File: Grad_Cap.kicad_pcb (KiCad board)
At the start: 2 copper layers, 339.4 x 339.4 mm, 89 parts, among them U1 ItsyBitsy 32u4 5V

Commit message: routing time
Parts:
- moved U1 48.4 mm to (202.5, 220.0), turned to 0 degrees
- renumbered D71 to D1, D4 to D10, D5 to D11, D7 to D12, D8 to D13, D9 to D14, D64 to D15, D63 to D16, D62 to D17, D61 to D18, D60 to D19, D70 to D2, D59 to D20, D58 to D21, D57 to D22, D56 to D23, D55 to D24, D54 to D25, D52 to D26, D51 to D27, D49 to D28, D48 to D29, D69 to D3, D48 to D30, D46 to D31, D45 to D32, D44 to D33, D43 to D34, D41 to D35, D40 to D36, D39 to D37, D37 to D39, D68 to D4, D36 to D40, D35 to D41, D33 to D42, D32 to D43, D31 to D44, D30 to D45, D29 to D46, D28 to D47, D27 to D48, D25 to D49, D67 to D5, D24 to D50, D23 to D51, D22 to D52, D21 to D53, D20 to D54, D19 to D55, D17 to D56, D16 to D57, D15 to D58, D14 to D59, D66 to D6, D13 to D60, D7 to D61, D8 to D62, D10 to D63, D11 to D64, D12 to D65, D1 to D66, D1 to D67, D65 to D68, D9 to D69, D65 to D7, D66 to D70, D65 to D71, D9 to D72, D66 to D73, D67 to D74, D9 to D75, D8 to D76, D7 to D77, D9 to D78, D9 to D79, D1 to D8, D9 to D80, D9 to D81, D9 to D82, D8 to D83, D7 to D84, D8 to D85, D3 to D9
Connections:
- D1 pad 2: Net-(D70-Pad4) -> Net-(D1-Pad2)
- D1 pad 4: Net-(D71-Pad4) -> Net-(D1-Pad4)
- D11 pad 4: Net-(D5-Pad4) -> Net-(D11-Pad4)
- D12 pad 2: Net-(D6-Pad4) -> Net-(D11-Pad4)
- D12 pad 4: Net-(D7-Pad4) -> Net-(D12-Pad4)
- D13 pad 2: Net-(D7-Pad4) -> Net-(D12-Pad4)
- D13 pad 4: Net-(D8-Pad4) -> Net-(D13-Pad4)
- D14 pad 1: (no net) -> GND
- D14 pad 2: (no net) -> Net-(D13-Pad4)
- D14 pad 3: (no net) -> +5V
- D14 pad 4: (no net) -> Net-(D14-Pad4)
- D15 pad 2: Net-(D63-Pad4) -> Net-(D14-Pad4)
- D15 pad 4: Net-(D64-Pad4) -> Net-(D15-Pad4)
- D16 pad 2: Net-(D62-Pad4) -> Net-(D15-Pad4)
- D16 pad 4: Net-(D63-Pad4) -> Net-(D16-Pad4)
- D17 pad 2: Net-(D61-Pad4) -> Net-(D16-Pad4)
- D17 pad 4: Net-(D62-Pad4) -> Net-(D17-Pad4)
- D18 pad 2: Net-(D60-Pad4) -> Net-(D17-Pad4)
- D18 pad 4: Net-(D61-Pad4) -> Net-(D18-Pad4)
- D19 pad 2: Net-(D59-Pad4) -> Net-(D18-Pad4)
- D19 pad 4: Net-(D60-Pad4) -> Net-(D19-Pad4)
- D2 pad 2: Net-(D69-Pad4) -> Net-(D1-Pad4)
- D2 pad 4: Net-(D70-Pad4) -> Net-(D2-Pad4)
- D20 pad 2: Net-(D58-Pad4) -> Net-(D19-Pad4)
- D20 pad 4: Net-(D59-Pad4) -> Net-(D20-Pad4)
- D21 pad 2: Net-(D57-Pad4) -> Net-(D20-Pad4)
- D21 pad 4: Net-(D58-Pad4) -> Net-(D21-Pad4)
- D22 pad 2: Net-(D56-Pad4) -> Net-(D21-Pad4)
- D22 pad 4: Net-(D57-Pad4) -> Net-(D22-Pad4)
- D23 pad 2: Net-(D55-Pad4) -> Net-(D22-Pad4)
- D23 pad 4: Net-(D56-Pad4) -> Net-(D23-Pad4)
- D24 pad 2: Net-(D54-Pad4) -> Net-(D23-Pad4)
- D24 pad 4: Net-(D55-Pad4) -> Net-(D24-Pad4)
- D25 pad 2: Net-(D53-Pad4) -> Net-(D24-Pad4)
- D25 pad 4: Net-(D54-Pad4) -> Net-(D25-Pad4)
- D26 pad 2: Net-(D51-Pad4) -> Net-(D25-Pad4)
- D26 pad 4: Net-(D52-Pad4) -> Net-(D26-Pad4)
- D27 pad 2: Net-(D50-Pad4) -> Net-(D26-Pad4)
- D27 pad 4: Net-(D51-Pad4) -> Net-(D27-Pad4)
- D28 pad 2: Net-(D48-Pad4) -> Net-(D27-Pad4)
- D28 pad 4: Net-(D49-Pad4) -> Net-(D28-Pad4)
- D29 pad 2: Net-(D47-Pad4) -> Net-(D28-Pad4)
- D29 pad 4: Net-(D48-Pad4) -> Net-(D29-Pad4)
- D3 pad 2: Net-(D68-Pad4) -> Net-(D2-Pad4)
- D3 pad 4: Net-(D69-Pad4) -> Net-(D3-Pad4)
- D30 pad 1: (no net) -> GND
- D30 pad 2: (no net) -> Net-(D29-Pad4)
- D30 pad 3: (no net) -> +5V
- D30 pad 4: (no net) -> Net-(D30-Pad4)
- D31 pad 2: Net-(D45-Pad4) -> Net-(D30-Pad4)
- D31 pad 4: Net-(D46-Pad4) -> Net-(D31-Pad4)
- D32 pad 2: Net-(D44-Pad4) -> Net-(D31-Pad4)
- D32 pad 4: Net-(D45-Pad4) -> Net-(D32-Pad4)
- D33 pad 2: Net-(D43-Pad4) -> Net-(D32-Pad4)
- D33 pad 4: Net-(D44-Pad4) -> Net-(D33-Pad4)
- D34 pad 2: Net-(D42-Pad4) -> Net-(D33-Pad4)
- D34 pad 4: Net-(D43-Pad4) -> Net-(D34-Pad4)
- D35 pad 2: Net-(D40-Pad4) -> Net-(D34-Pad4)
- D35 pad 4: Net-(D41-Pad4) -> Net-(D35-Pad4)
- D36 pad 2: Net-(D39-Pad4) -> Net-(D35-Pad4)
- D36 pad 4: Net-(D40-Pad4) -> Net-(D36-Pad4)
- D37 pad 2: Net-(D38-Pad4) -> Net-(D36-Pad4)
- D37 pad 4: Net-(D39-Pad4) -> Net-(D37-Pad4)
- D39 pad 2: Net-(D36-Pad4) -> Net-(D38-Pad4)
- D39 pad 4: Net-(D37-Pad4) -> Net-(D39-Pad4)
- D4 pad 2: Net-(D67-Pad4) -> Net-(D3-Pad4)
- D4 pad 4: Net-(D68-Pad4) -> Net-(D4-Pad4)
- D40 pad 2: Net-(D35-Pad4) -> Net-(D39-Pad4)
- D40 pad 4: Net-(D36-Pad4) -> Net-(D40-Pad4)
- D41 pad 2: Net-(D34-Pad4) -> Net-(D40-Pad4)
- D41 pad 4: Net-(D35-Pad4) -> Net-(D41-Pad4)
- D42 pad 2: Net-(D32-Pad4) -> Net-(D41-Pad4)
- D42 pad 4: Net-(D33-Pad4) -> Net-(D42-Pad4)
- D43 pad 2: Net-(D31-Pad4) -> Net-(D42-Pad4)
- D43 pad 4: Net-(D32-Pad4) -> Net-(D43-Pad4)
- D44 pad 2: Net-(D30-Pad4) -> Net-(D43-Pad4)
- D44 pad 4: Net-(D31-Pad4) -> Net-(D44-Pad4)
- D45 pad 2: Net-(D29-Pad4) -> Net-(D44-Pad4)
- D45 pad 4: Net-(D30-Pad4) -> Net-(D45-Pad4)
- D46 pad 2: Net-(D28-Pad4) -> Net-(D45-Pad4)
- D46 pad 4: Net-(D29-Pad4) -> Net-(D46-Pad4)
- D47 pad 2: Net-(D27-Pad4) -> Net-(D46-Pad4)
- D47 pad 4: Net-(D28-Pad4) -> Net-(D47-Pad4)
- D48 pad 2: Net-(D26-Pad4) -> Net-(D47-Pad4)
- D48 pad 4: Net-(D27-Pad4) -> Net-(D48-Pad4)
- D49 pad 2: Net-(D24-Pad4) -> Net-(D48-Pad4)
- D49 pad 4: Net-(D25-Pad4) -> Net-(D49-Pad4)
- D5 pad 2: Net-(D66-Pad4) -> Net-(D4-Pad4)
- D5 pad 4: Net-(D67-Pad4) -> Net-(D5-Pad4)
- D50 pad 2: Net-(D23-Pad4) -> Net-(D49-Pad4)
- D50 pad 4: Net-(D24-Pad4) -> Net-(D50-Pad4)
- D51 pad 1: (no net) -> GND
- D51 pad 2: (no net) -> Net-(D50-Pad4)
- D51 pad 3: (no net) -> +5V
- D51 pad 4: (no net) -> Net-(D51-Pad4)
- D52 pad 2: Net-(D21-Pad4) -> Net-(D51-Pad4)
- D52 pad 4: Net-(D22-Pad4) -> Net-(D52-Pad4)
- D53 pad 2: Net-(D20-Pad4) -> Net-(D52-Pad4)
- D53 pad 4: Net-(D21-Pad4) -> Net-(D53-Pad4)
- D54 pad 2: Net-(D19-Pad4) -> Net-(D53-Pad4)
- D54 pad 4: Net-(D20-Pad4) -> Net-(D54-Pad4)
- D55 pad 2: Net-(D18-Pad4) -> Net-(D54-Pad4)
- D55 pad 4: Net-(D19-Pad4) -> Net-(D55-Pad4)
- D56 pad 2: Net-(D16-Pad4) -> Net-(D55-Pad4)
- D56 pad 4: Net-(D17-Pad4) -> Net-(D56-Pad4)
- D57 pad 2: Net-(D15-Pad4) -> Net-(D56-Pad4)
- D57 pad 4: Net-(D16-Pad4) -> Net-(D57-Pad4)
- D58 pad 2: Net-(D14-Pad4) -> Net-(D57-Pad4)
- D58 pad 4: Net-(D15-Pad4) -> Net-(D58-Pad4)
- D59 pad 2: Net-(D13-Pad4) -> Net-(D58-Pad4)
- D59 pad 4: Net-(D14-Pad4) -> Net-(D59-Pad4)
- D6 pad 2: Net-(D65-Pad4) -> Net-(D5-Pad4)
- D6 pad 4: Net-(D66-Pad4) -> Net-(D6-Pad4)
- D60 pad 2: Net-(D12-Pad4) -> Net-(D59-Pad4)
- D60 pad 4: Net-(D13-Pad4) -> Net-(D60-Pad4)
- D61 pad 2: Net-(D6-Pad4) -> Net-(D60-Pad4)
- D61 pad 4: Net-(D7-Pad4) -> Net-(D61-Pad4)
- D62 pad 2: Net-(D7-Pad4) -> Net-(D61-Pad4)
- D62 pad 4: Net-(D8-Pad4) -> Net-(D62-Pad4)
- D63 pad 2: Net-(D10-Pad2) (its old number) -> Net-(D62-Pad4)
- D63 pad 4: Net-(D10-Pad4) (its old number) -> Net-(D63-Pad4)
- D64 pad 1: (no net) -> GND
- D64 pad 2: (no net) -> Net-(D63-Pad4)
- D64 pad 3: (no net) -> +5V
- D64 pad 4: (no net) -> Net-(D64-Pad4)
- D65 pad 2: Net-(D11-Pad4) -> Net-(D64-Pad4)
- D65 pad 4: Net-(D12-Pad4) -> Net-(D65-Pad4)
- D66 pad 1: (no net) -> GND
- D66 pad 2: (no net) -> Net-(D65-Pad4)
- D66 pad 3: (no net) -> +5V
- D66 pad 4: (no net) -> Net-(D66-Pad4)
- D67 pad 1: (no net) -> GND
- D67 pad 2: (no net) -> Net-(D66-Pad4)
- D67 pad 3: (no net) -> +5V
- D67 pad 4: (no net) -> Net-(D67-Pad4)
- D68 pad 2: Net-(D64-Pad4) -> Net-(D67-Pad4)
- D68 pad 4: Net-(D65-Pad4) -> Net-(D68-Pad4)
- D69 pad 1: (no net) -> GND
- D69 pad 2: (no net) -> Net-(D68-Pad4)
- D69 pad 3: (no net) -> +5V
- D69 pad 4: (no net) -> Net-(D69-Pad4)
- D7 pad 2: Net-(D64-Pad4) -> Net-(D6-Pad4)
- D7 pad 4: Net-(D65-Pad4) -> Net-(D7-Pad4)
- D70 pad 2: Net-(D65-Pad4) -> Net-(D69-Pad4)
- D70 pad 4: Net-(D66-Pad4) -> Net-(D70-Pad4)
- D71 pad 2: Net-(D64-Pad4) -> Net-(D70-Pad4)
- D71 pad 4: Net-(D65-Pad4) -> Net-(D71-Pad4)
- D72 pad 1: (no net) -> GND
- D72 pad 2: (no net) -> Net-(D71-Pad4)
- D72 pad 3: (no net) -> +5V
- D72 pad 4: (no net) -> unconnected-(D72-Pad4)
- D8 pad 2: Net-(D1-Pad2) -> Net-(D7-Pad4)
- D8 pad 4: Net-(D1-Pad4) -> Net-(D8-Pad4)
- D9 pad 2: Net-(D2-Pad4) -> Net-(D8-Pad4)
- R1 pad 1: Net-(R1-Pad1) -> Net-(U1-Pad19)
- U1 pad 19: unconnected-(U1-Pad19) -> Net-(U1-Pad19)
- U1 pad 25: Net-(R1-Pad1) -> unconnected-(U1-Pad25)

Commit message: ground vias?
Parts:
- removed D37: Neopixel 5050, LED_SMD:LED_Inolux_IN-PI554FCH_PLCC4_5.0x5.0mm_P3.2mm
- moved R1 123.3 mm to (233.8, 237.8), turned to -90 degrees
- turned D41 to 180 degrees
- turned D42 to 180 degrees
- turned D1 to 180 degrees
- turned D14 to 180 degrees
- turned D15 to 180 degrees
- turned D16 to 180 degrees
- turned D17 to 180 degrees
- turned D18 to 180 degrees
- turned D19 to 180 degrees
- turned D2 to 180 degrees
- turned D20 to 180 degrees
- turned D3 to 180 degrees
- turned D40 to 180 degrees
- turned D43 to 180 degrees
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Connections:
- D38 pad 2: Net-(D37-Pad4) -> Net-(D36-Pad4)
- D72 pad 4: unconnected-(D72-Pad4) -> Net-(D72-Pad4)
- D73 pad 2: Net-(D65-Pad4) -> Net-(D72-Pad4)
- D73 pad 4: Net-(D66-Pad4) -> Net-(D73-Pad4)
- D74 pad 2: Net-(D66-Pad4) -> Net-(D73-Pad4)
- D74 pad 4: Net-(D67-Pad4) -> Net-(D74-Pad4)
- D75 pad 1: (no net) -> GND
- D75 pad 2: (no net) -> Net-(D74-Pad4)
- D75 pad 3: (no net) -> +5V
- D75 pad 4: (no net) -> Net-(D75-Pad4)
- D76 pad 2: Net-(D7-Pad4) -> Net-(D75-Pad4)
- D76 pad 4: Net-(D8-Pad4) -> Net-(D76-Pad4)
- D77 pad 2: Net-(D6-Pad4) -> Net-(D76-Pad4)
- D77 pad 4: Net-(D7-Pad4) -> Net-(D77-Pad4)
- D78 pad 1: (no net) -> GND
- D78 pad 2: (no net) -> Net-(D77-Pad4)
- D78 pad 3: (no net) -> +5V
- D78 pad 4: (no net) -> Net-(D78-Pad4)
- D79 pad 1: (no net) -> GND
- D79 pad 2: (no net) -> Net-(D78-Pad4)
- D79 pad 3: (no net) -> +5V
- D79 pad 4: (no net) -> Net-(D79-Pad4)
- D80 pad 1: (no net) -> GND
- D80 pad 2: (no net) -> Net-(D79-Pad4)
- D80 pad 3: (no net) -> +5V
- D80 pad 4: (no net) -> Net-(D80-Pad4)
- D81 pad 1: (no net) -> GND
- D81 pad 2: (no net) -> Net-(D80-Pad4)
- D81 pad 3: (no net) -> +5V
- D81 pad 4: (no net) -> Net-(D81-Pad4)
- D82 pad 1: (no net) -> GND
- D82 pad 2: (no net) -> Net-(D81-Pad4)
- D82 pad 3: (no net) -> +5V
- D82 pad 4: (no net) -> Net-(D82-Pad4)
- D83 pad 2: Net-(D7-Pad4) -> Net-(D82-Pad4)
- D83 pad 4: Net-(D8-Pad4) -> Net-(D83-Pad4)
- D84 pad 2: Net-(D6-Pad4) -> Net-(D83-Pad4)
- D84 pad 4: Net-(D7-Pad4) -> Net-(D84-Pad4)
- D85 pad 2: Net-(D7-Pad4) -> Net-(D84-Pad4)
- D85 pad 4: Net-(D8-Pad4) -> Net-(D85-Pad4)
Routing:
- net Net-(D60-Pad4): track 0.00 -> 50.6 mm
- net Net-(R1-Pad1): track 0.00 -> 21.2 mm
- net Net-(D81-Pad4): track 0.00 -> 19.1 mm
- net Net-(D79-Pad4): track 0.00 -> 18.8 mm
- net Net-(D48-Pad4): track 0.00 -> 16.6 mm
- net Net-(D61-Pad4): track 0.00 -> 14.4 mm
- net Net-(D8-Pad4): track 0.00 -> 14.3 mm
- net Net-(D64-Pad4): track 0.00 -> 13.7 mm
- net Net-(D13-Pad4): track 0.00 -> 13.4 mm
- net Net-(D75-Pad4): track 0.00 -> 13.1 mm
- net Net-(D4-Pad4): track 0.00 -> 12.9 mm
- net Net-(D39-Pad4): track 0.00 -> 12.9 mm
- net Net-(D47-Pad4): track 0.00 -> 12.4 mm
- net Net-(D62-Pad4): track 0.00 -> 12.3 mm
- net Net-(D21-Pad4): track 0.00 -> 12.0 mm
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- added copper zone on F.Cu, net +5V
- added copper zone on B.Cu, net GND

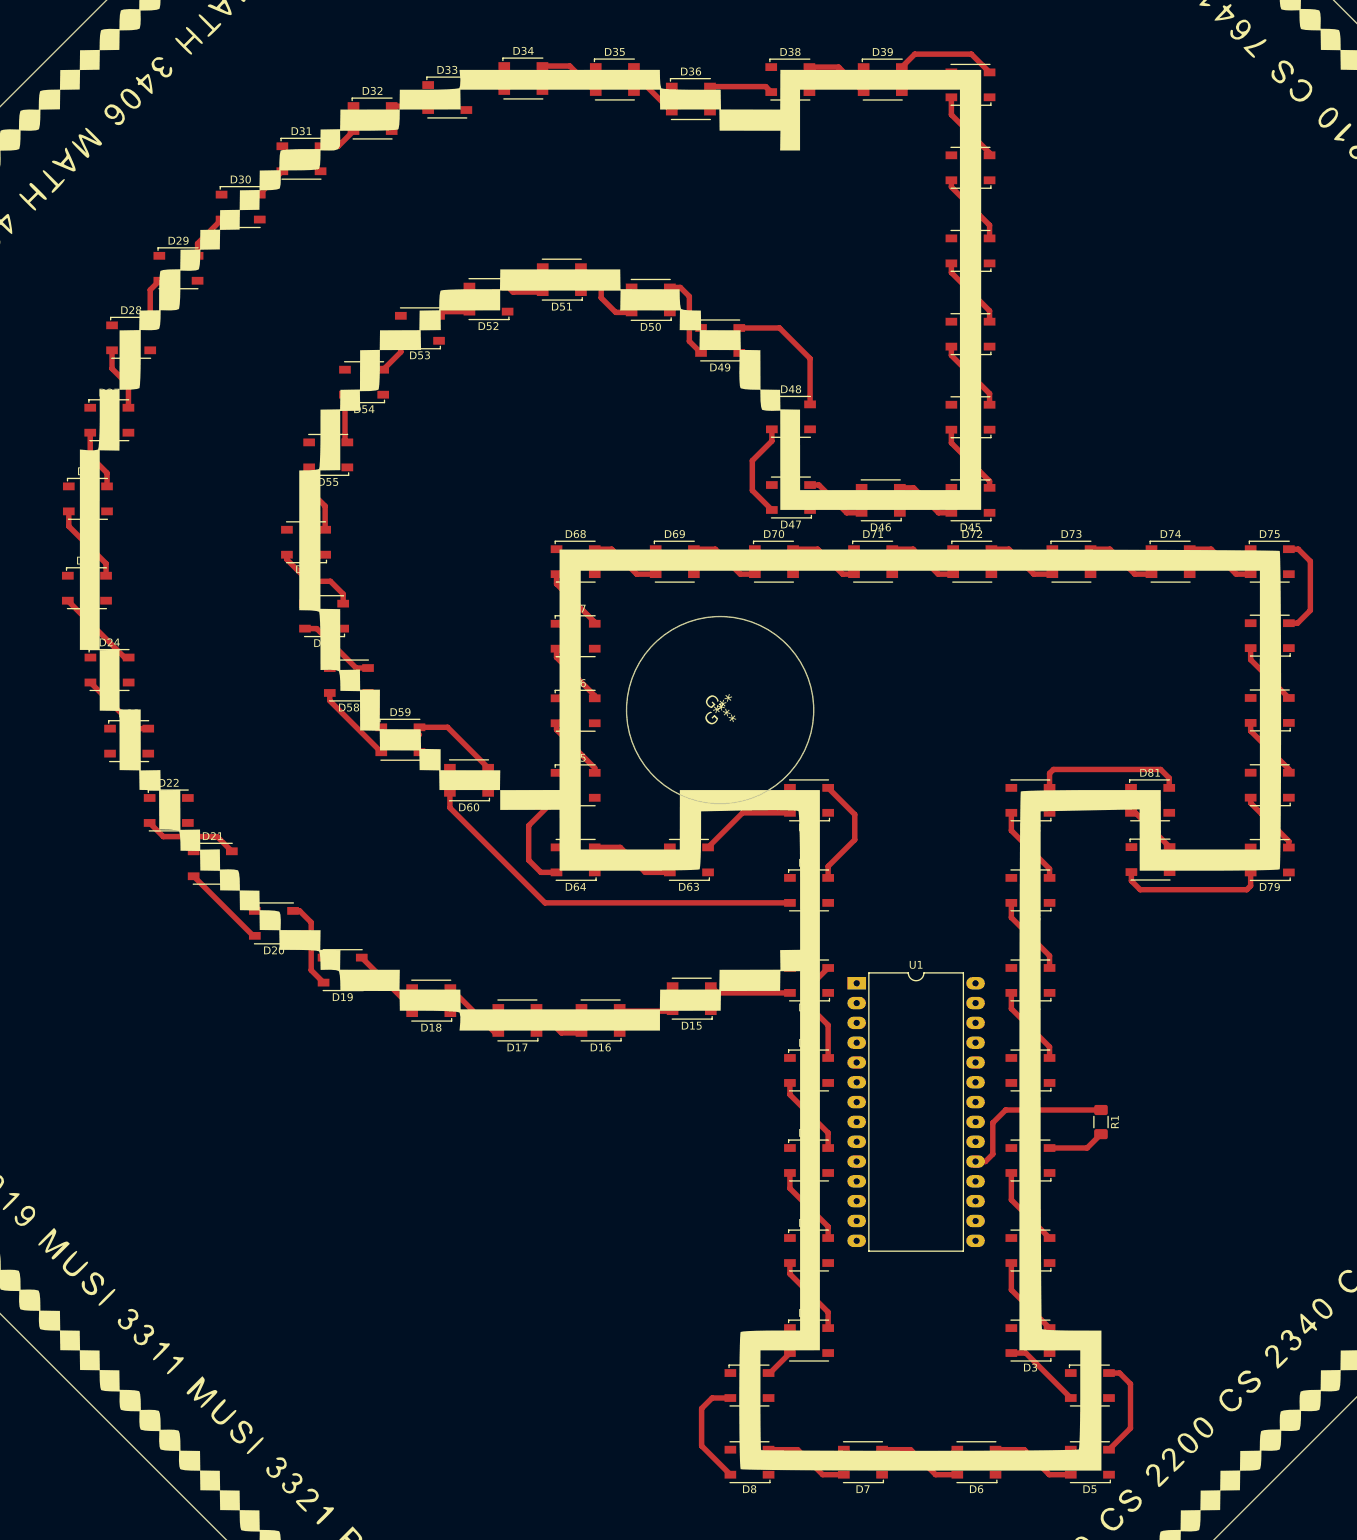
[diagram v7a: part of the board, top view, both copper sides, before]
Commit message: Routing and pours done
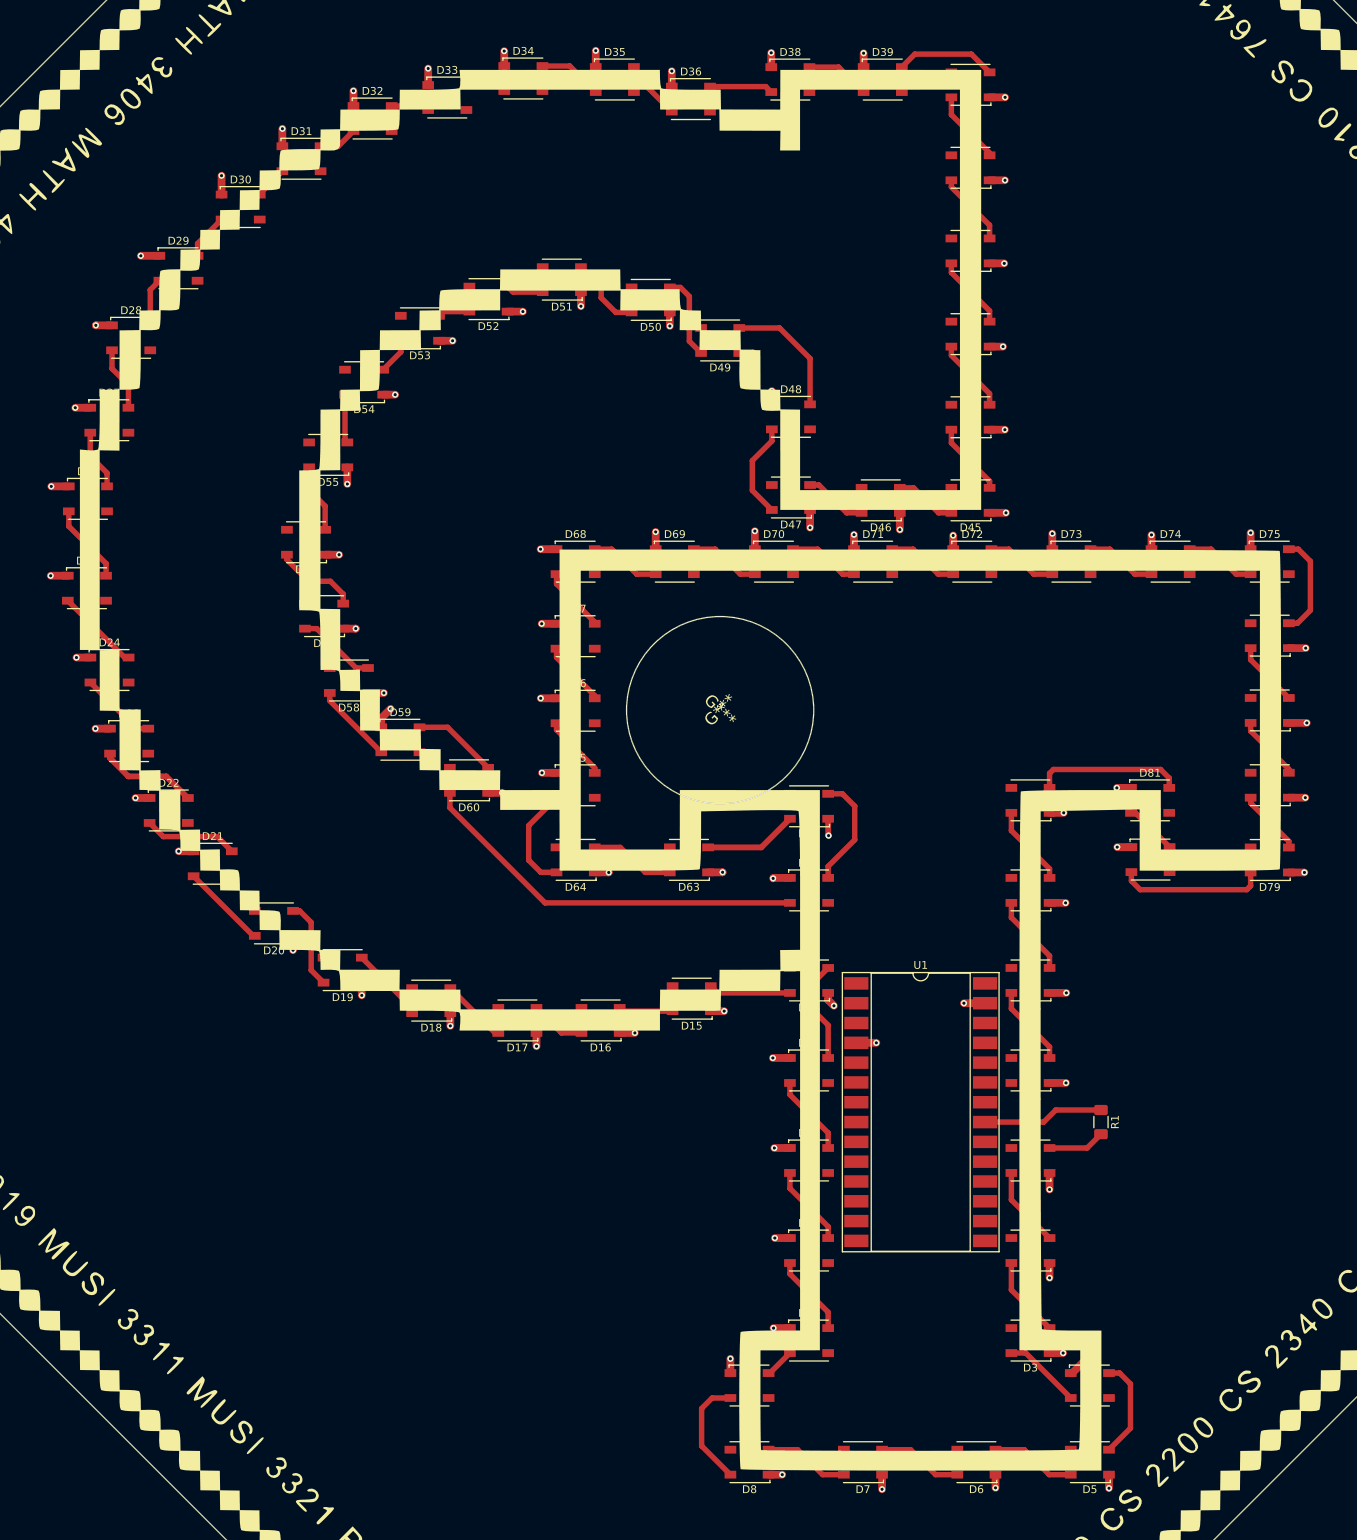
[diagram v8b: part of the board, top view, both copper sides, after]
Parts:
- U1: footprint Package_DIP:DIP-28_W15.24mm_LongPads -> Package_DIP:DIP-28_W16.51mm_SMDSocket_LongPads
- moved U1 18.5 mm to (210.7, 236.6)
- moved D62 0.76 mm to (196.4, 197.3)
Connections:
- D85 pad 4: Net-(D85-Pad4) -> unconnected-(D85-Pad4)
- U1 pad 19: Net-(R1-Pad1) -> unconnected-(U1-Pad19)
- U1 pad 21: unconnected-(U1-Pad21) -> Net-(R1-Pad1)
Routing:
- net GND: track 0.00 -> 170.8 mm, vias 0 -> 86
- net Net-(D22-Pad4): track 0.00 -> 12.7 mm
- net Net-(R1-Pad1): track 21.2 -> 15.5 mm
- net unconnected-(U1-Pad19): track 0.00 -> 1.27 mm
